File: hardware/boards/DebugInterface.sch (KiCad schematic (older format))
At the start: 1 part, among them U1 ECP5UM5G-381caBGA

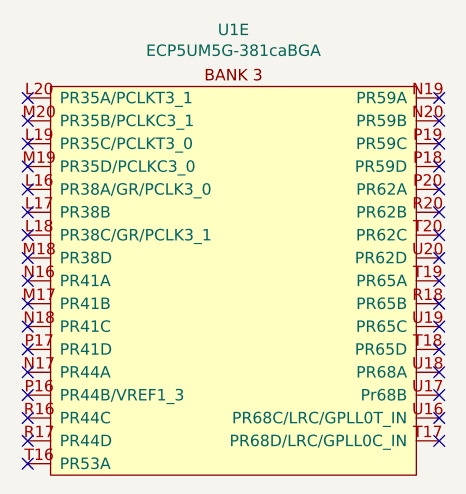
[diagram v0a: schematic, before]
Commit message: Added the main OSC for the FPGA
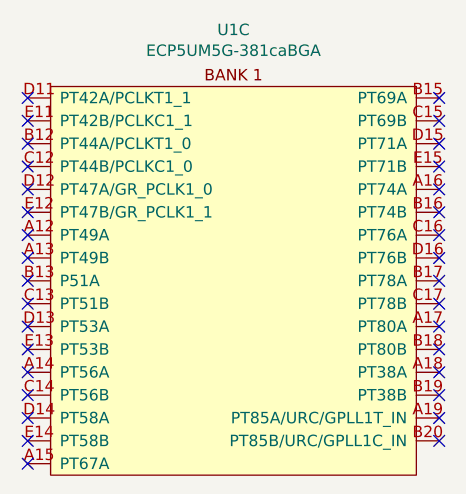
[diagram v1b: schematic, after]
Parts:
- removed U1: ECP5UM5G-381caBGA, lethalbit:318caBGA, symbol lethalbit:ECP5UM5G-381caBGA
- added U1: ECP5UM5G-381caBGA, lethalbit:318caBGA, symbol lethalbit:ECP5UM5G-381caBGA
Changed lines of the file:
@@
 $Descr A3 16535 11693
 encoding utf-8
-Sheet 5 11
+Sheet 3 11
 Title "lethallink"
 Date "2020-06-13"
@@
 Comment4 ""
 $EndDescr
-$Comp
-L lethalbit:ECP5UM5G-381caBGA U1
-U 5 1 5F210C09
-P 5850 3150
-F 0 "U1" H 5850 3498 50  0000 C CNN
-F 1 "ECP5UM5G-381caBGA" H 5850 3407 50  0000 C CNN
-F 2 "lethalbit:318caBGA" H 4500 3300 50  0001 C CNN
-F 3 "" H 4500 3300 50  0001 C CNN
-F 4 "Lattice" H 5850 3150 50  0001 C CNN "MFR"
-F 5 "LFE5UM5G-85F-8BG381I" H 5850 3150 50  0001 C CNN "MPN"
-F 6 "220-2112-ND" H 5850 3150 50  0001 C CNN "DIGIKEY_PN"
-	5    5850 3150
-	1    0    0    -1
-$EndComp
 NoConn ~ 4950 3100
 NoConn ~ 4950 3200
@@
 NoConn ~ 6750 3200
 NoConn ~ 6750 3100
+$Comp
+L lethalbit:ECP5UM5G-381caBGA U?
+U 3 1 610DED19
+P 5850 3150
+AR Path="/610DED19" Ref="U?"  Part="3"
+AR Path="/5F2CAFD2/610DED19" Ref="U?"  Part="3"
+AR Path="/5EF67D90/610DED19" Ref="U1"  Part="3"
+F 0 "U1" H 5850 3498 50  0000 C CNN
+F 1 "ECP5UM5G-381caBGA" H 5850 3407 50  0000 C CNN
+F 2 "lethalbit:318caBGA" H 4500 3300 50  0001 C CNN
+F 3 "" H 4500 3300 50  0001 C CNN
+F 4 "Lattice" H 5850 3150 50  0001 C CNN "MFR"
+F 5 "LFE5UM5G-85F-8BG381I" H 5850 3150 50  0001 C CNN "MPN"
+F 6 "220-2112-ND" H 5850 3150 50  0001 C CNN "DIGIKEY_PN"
+	3    5850 3150
+	1    0    0    -1
+$EndComp
 $EndSCHEMATC

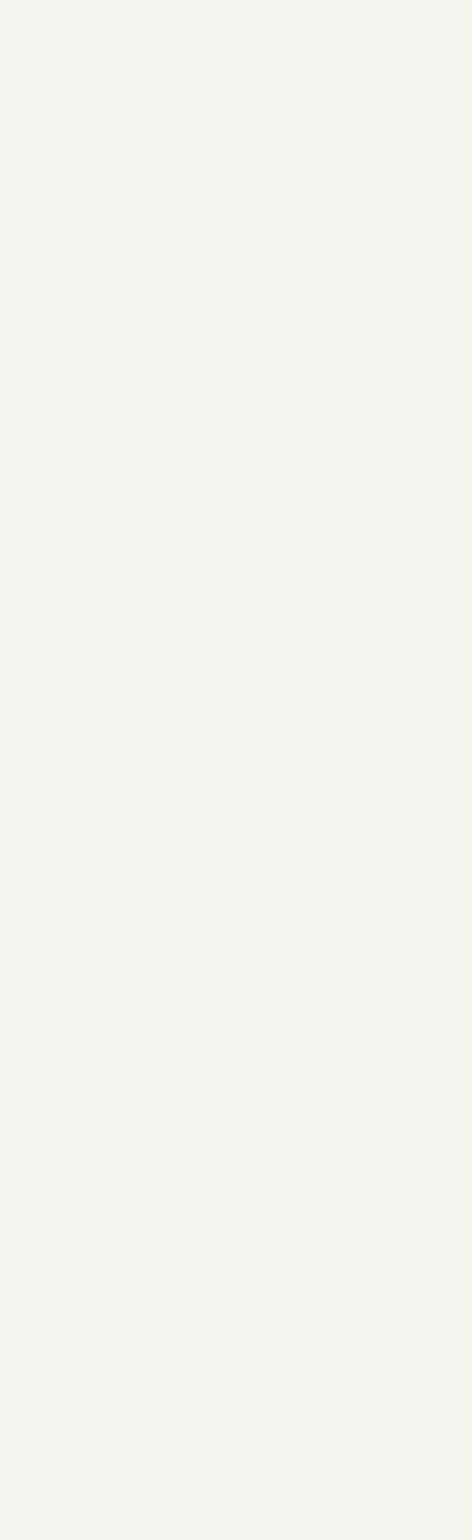
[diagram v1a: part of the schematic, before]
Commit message: Added the debug module connector (SODIMM 260), it's not hooked up to anything yet
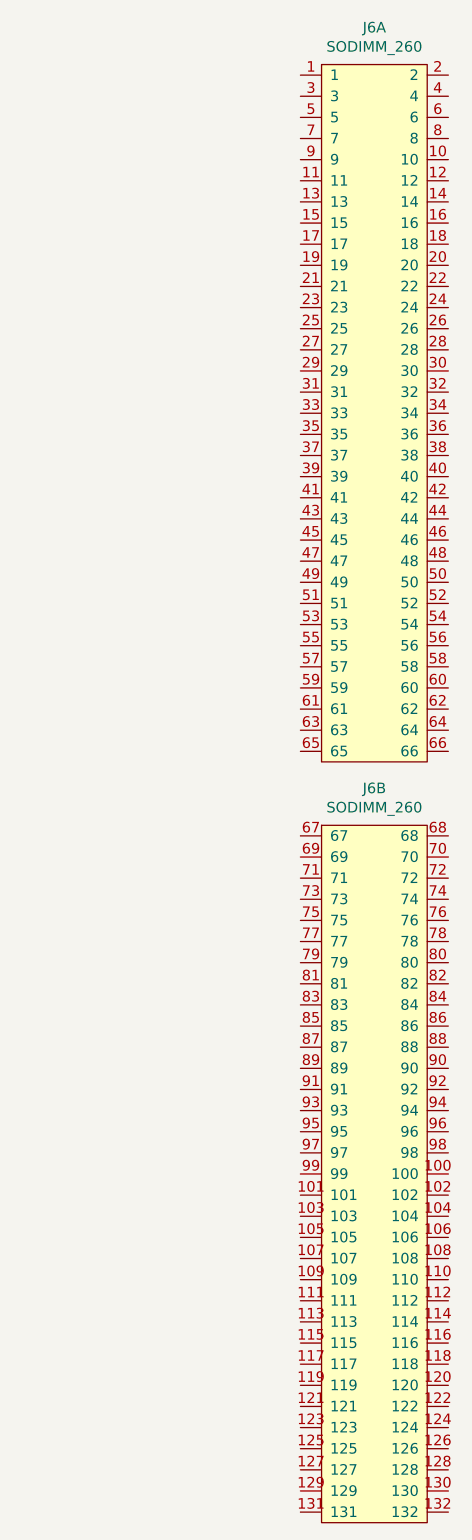
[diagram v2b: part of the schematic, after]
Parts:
- added J6: SODIMM_260, lethalbit-connectors:TE_SODIMM_260, symbol lethalbit:SODIMM_260
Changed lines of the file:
@@
 NoConn ~ 4950 4600
 NoConn ~ 4950 4700
-NoConn ~ 6750 4600
 NoConn ~ 6750 4500
 NoConn ~ 6750 4400
@@
 	1    0    0    -1
 $EndComp
+NoConn ~ 6750 4600
+$Comp
+L lethalbit:SODIMM_260 J6
+U 1 1 5F29016C
+P 10100 1850
+F 0 "J6" H 10100 2425 50  0000 C CNN
+F 1 "SODIMM_260" H 10100 2334 50  0000 C CNN
+F 2 "lethalbit-connectors:TE_SODIMM_260" H 10100 2200 50  0001 C CNN
+F 3 "https://www.te.com/commerce/DocumentDelivery/DDEController?Action=srchrtrv&DocNm=2309413&DocType=Customer+Drawing&DocLang=English" H 10100 2200 50  0001 C CNN
+F 4 "TE Connectivity AMP Connectors" H 10100 1850 50  0001 C CNN "MFR"
+F 5 "2309413-1" H 10100 1850 50  0001 C CNN "MPN"
+	1    10100 1850
+	1    0    0    -1
+$EndComp
+$Comp
+L lethalbit:SODIMM_260 J6
+U 2 1 5F297503
+P 10100 5450
+F 0 "J6" H 10100 6025 50  0000 C CNN
+F 1 "SODIMM_260" H 10100 5934 50  0000 C CNN
+F 2 "lethalbit-connectors:TE_SODIMM_260" H 10100 5800 50  0001 C CNN
+F 3 "https://www.te.com/commerce/DocumentDelivery/DDEController?Action=srchrtrv&DocNm=2309413&DocType=Customer+Drawing&DocLang=English" H 10100 5800 50  0001 C CNN
+F 4 "TE connectivity AMP Connectors" H 10100 5450 50  0001 C CNN "MFR"
+F 5 "2309413-1" H 10100 5450 50  0001 C CNN "MPN"
+	2    10100 5450
+	1    0    0    -1
+$EndComp
